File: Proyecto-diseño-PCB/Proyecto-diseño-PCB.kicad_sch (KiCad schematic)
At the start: 28 parts, among them J1 PROGRAMACIÓN/DEPURACIÓN, J2 USB_B_Micro, J3 Conn_01x13_Pin, J4 Conn_01x13_Pin, SW1 RESET, SW2 BOTON, SW3 BOTON, U1 PIC18LF45K50-I/P, U2 LP2950-3.3_TO92

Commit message: Correcciones
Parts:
- removed C7, C8: 1n, symbol Device:C
- added D4, D5: PESD3V3L4UG, Package_TO_SOT_SMD:SOT-353_SC-70-5, symbol Power_Protection:PESD3V3L4UG
- added FL1: BNX025, Filter:Filter_Murata_BNX025, symbol Filter:BNX025
- added R10, R11, R12, R13, R8, R9: 100, symbol Device:R_US
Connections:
- net BOTON1: now also D5.3 (K2), R8.2; no longer R6.1, SW2.1
- net BOTON2: now also D5.4 (K3), R9.2; no longer R7.1, SW3.1
- net GND: now also D4.2 (A), D5.2 (A), FL1.4 (CG); no longer J2.5 (GND)
- net MCLR: now also JP1.2 (B), R1.2, SW1.2, D5.1 (K1); no longer U1.1 (MCLR/VPP/RE3)
- net PGC: now also D4.4 (K3), R11.2; no longer J1.5 (Pin_5)
- net PGD: now also D4.5 (K4), R10.2; no longer J1.4 (Pin_4)
- net at J2.2 (D-): now also R12.2; no longer U1.23 (D-)
- net at J2.3 (D+): now also R13.2; no longer U1.24 (D+)
- net VIN: no longer names the net of C4.2, U2.3 (VI)
- net VIN: now also FL1.2 (CB); no longer J2.1 (VBUS), J3.14 (Pin_14)
- new net: R7.1, R9.1, SW3.1
- new net: R2.1, U1.1 (MCLR/VPP/RE3)
- new net: D4.3 (K2), R13.1, U1.24 (D+)
- new net: J1.4 (Pin_4), R10.1
- new net: J1.5 (Pin_5), R11.1
- new net: D4.1 (K1), R12.1, U1.23 (D-)
- new net: R6.1, R8.1, SW2.1
- new net 5V: FL1.1 (B), J2.1 (VBUS), J3.14 (Pin_14)
- new net MASA_SIN_FILTRAR: FL1.3 (PSG), J2.5 (GND)
- no-connect marks 1 -> 2
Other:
- note added: "Conectado a masa internamente"
- note added: "El PESD3V3L4UG es un integrado que cuenta con 4 TVS conectados a un anodo común. La conexión a masa solo está reperesntada en la unidad D#A."
- note removed: "Constante de tiempo DEBOUNCE = 100us"
- moved on the sheet: C4, C5, J2, R6, R7, SW2, SW3, U2

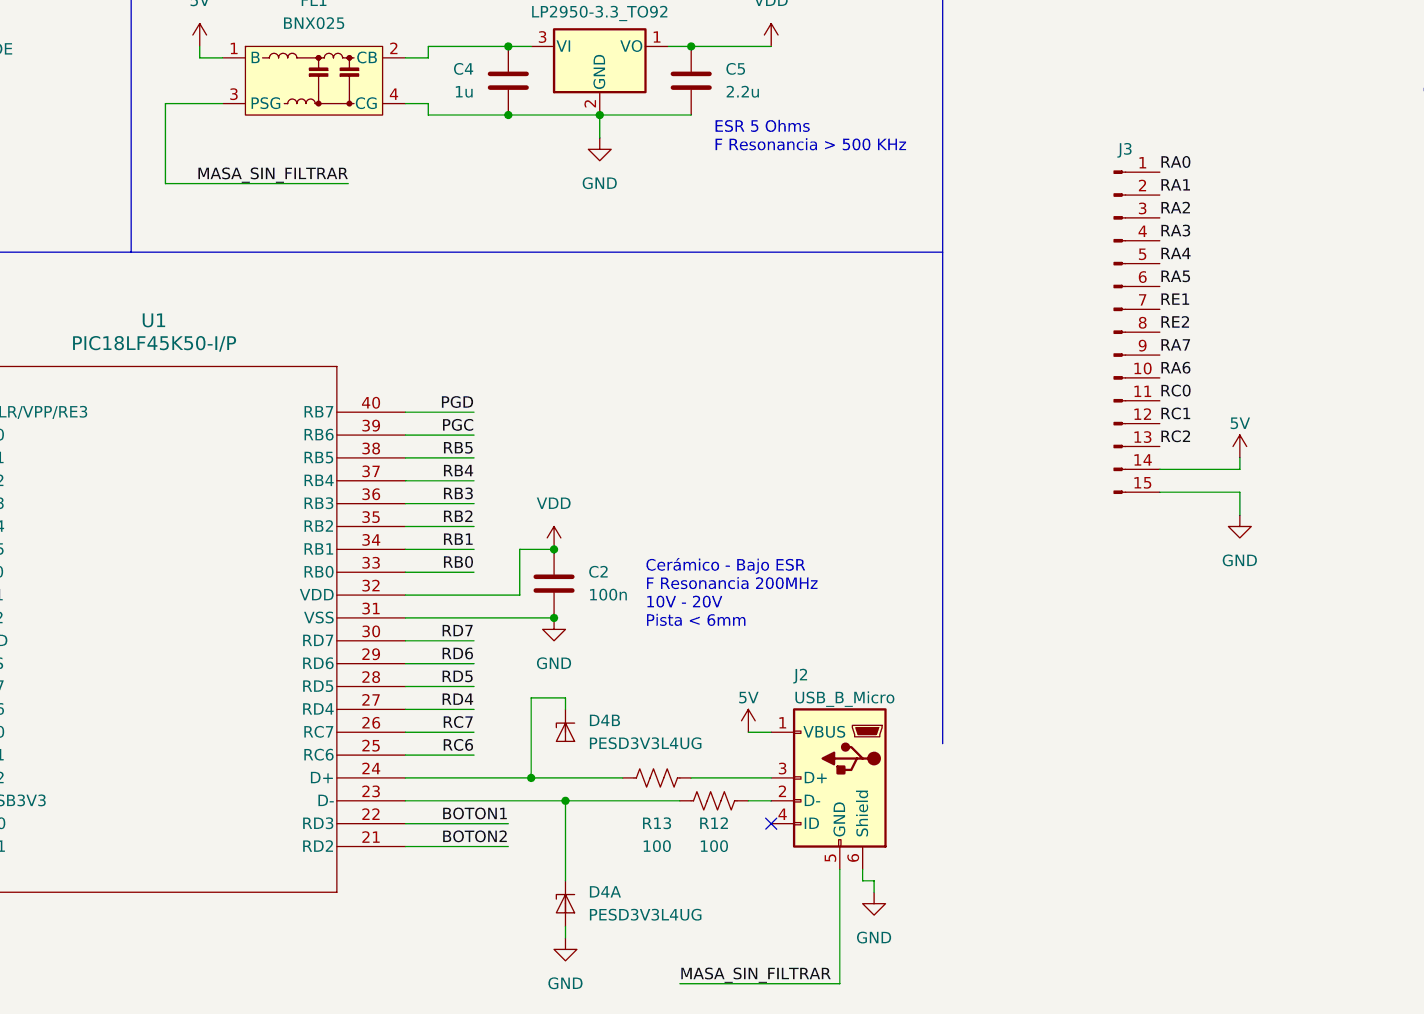
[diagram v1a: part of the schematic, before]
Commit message: fix: Cambio de nombre de net label
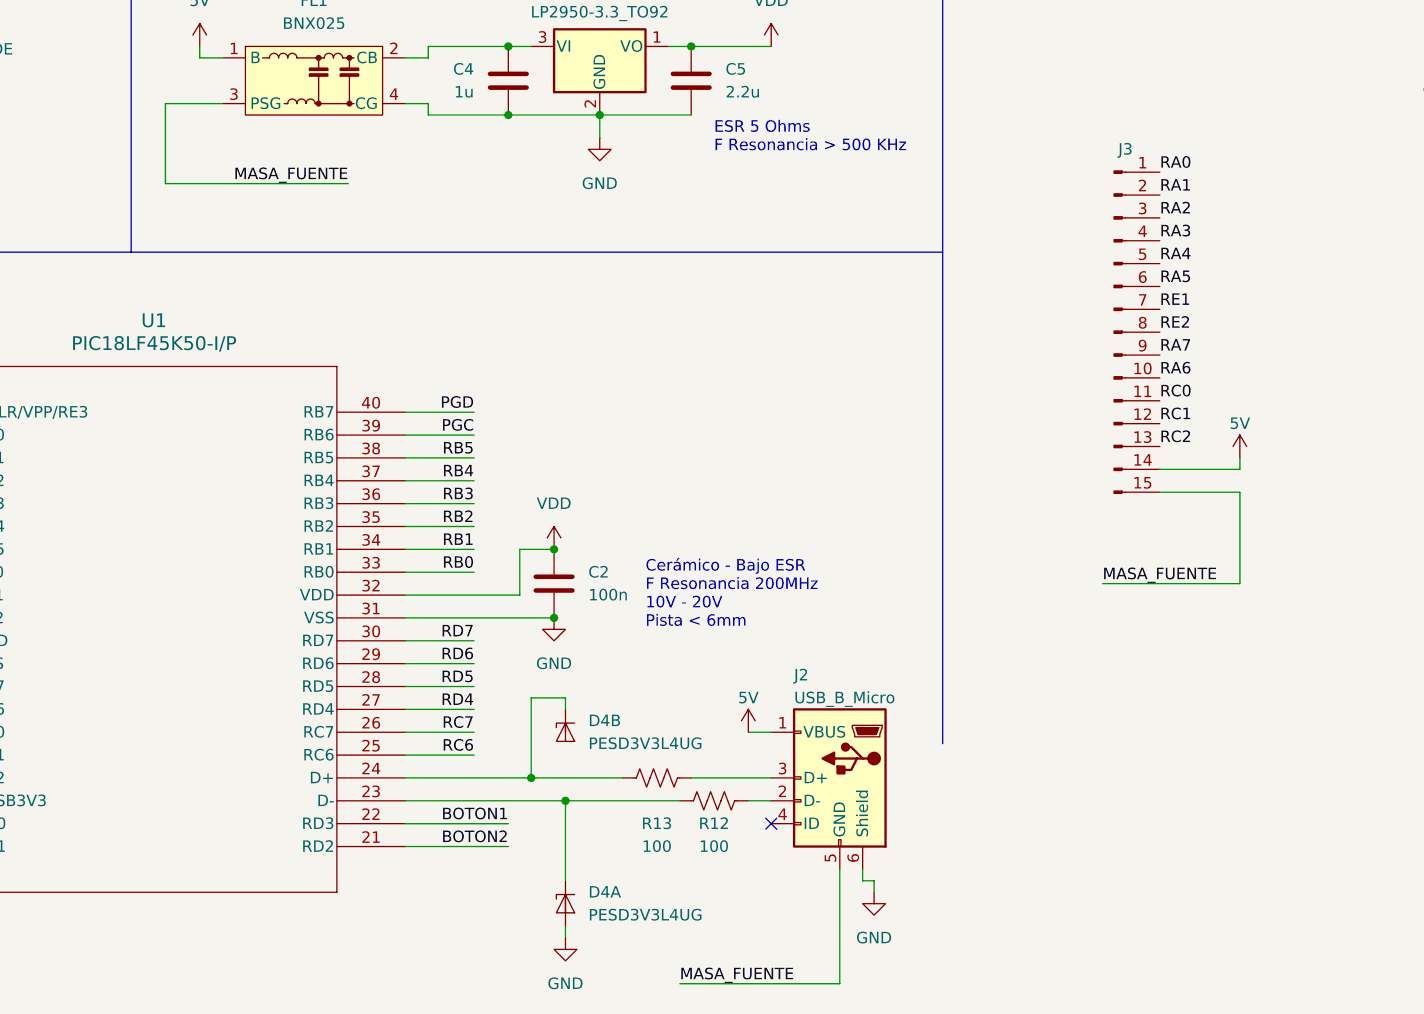
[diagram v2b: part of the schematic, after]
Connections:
- net GND: no longer J3.15 (Pin_15)
- net MASA_SIN_FILTRAR renamed MASA_FUENTE
- net MASA_FUENTE: now also J3.15 (Pin_15)
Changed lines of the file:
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@@
 	(wire
 		(pts
+			(xy 195.58 147.32) (xy 210.82 147.32)
+		)
+		(stroke
+			(width 0)
+			(type default)
+		)
+	)
+	(wire
+		(pts
 			(xy 53.34 173.99) (xy 62.23 173.99)
 		)
@@
 	(wire
 		(pts
-			(xy 210.82 137.16) (xy 210.82 139.7)
+			(xy 210.82 137.16) (xy 210.82 147.32)
 		)
 		(stroke
@@
 		)
 	)
-	(label "MASA_SIN_FILTRAR"
+	(label "MASA_FUENTE"
 		(at 148.59 191.77 0)
 		(effects
@@
 		)
 	)
-	(label "MASA_SIN_FILTRAR"
+	(label "MASA_FUENTE"
 		(at 111.76 102.87 180)
 		(effects
@@
 		)
 	)
+	(label "MASA_FUENTE"
+		(at 195.58 147.32 0)
+		(fields_autoplaced yes)
+		(effects
+			(font
+				(size 1.27 1.27)
+			)
+			(justify left bottom)
+		)
+		(property "Netclass" "ALIMENTACION"
+			(at 195.58 148.59 0)
+			(effects
+				(font
+					(size 1.27 1.27)
+					(italic yes)
+				)
+				(justify left)
+				(hide yes)
+			)
+		)
+	)
 	(label "RC2"
 		(at 54.61 168.91 0)
@@
 					(unit 1)
 				)
-			)
-		)
-	)
-	(symbol
-		(lib_id "power:GND")
-		(at 210.82 139.7 0)
-		(unit 1)
-		(exclude_from_sim no)
-		(in_bom yes)
-		(on_board yes)
-		(dnp no)
-		(fields_autoplaced yes)
-		(property "Reference" "#PWR025"
-			(at 210.82 146.05 0)
-			(effects
-				(font
-					(size 1.27 1.27)
-				)
-				(hide yes)
-			)
-		)
-		(property "Value" "GND"
-			(at 210.82 144.78 0)
-			(effects
-				(font
-					(size 1.27 1.27)
-				)
-			)
-		)
-		(property "Footprint" ""
-			(at 210.82 139.7 0)
-			(effects
-				(font
-					(size 1.27 1.27)
-				)
-				(hide yes)
-			)
-		)
-		(property "Datasheet" ""
-			(at 210.82 139.7 0)
-			(effects
-				(font
-					(size 1.27 1.27)
-				)
-				(hide yes)
-			)
-		)
-		(property "Description" "Power symbol creates a global label with name \"GND\" , ground"
-			(at 210.82 139.7 0)
-			(effects
-				(font
-					(size 1.27 1.27)
-				)
-				(hide yes)
-			)
-		)
-		(pin "1"
-		)
-		(instances
-			(project "Proyecto-diseño-PCB"
-				(path "/07fbb56e-f9f5-495b-a4b8-be8a0cd3547b"
-					(reference "#PWR025")
-					(unit 1)
-				)

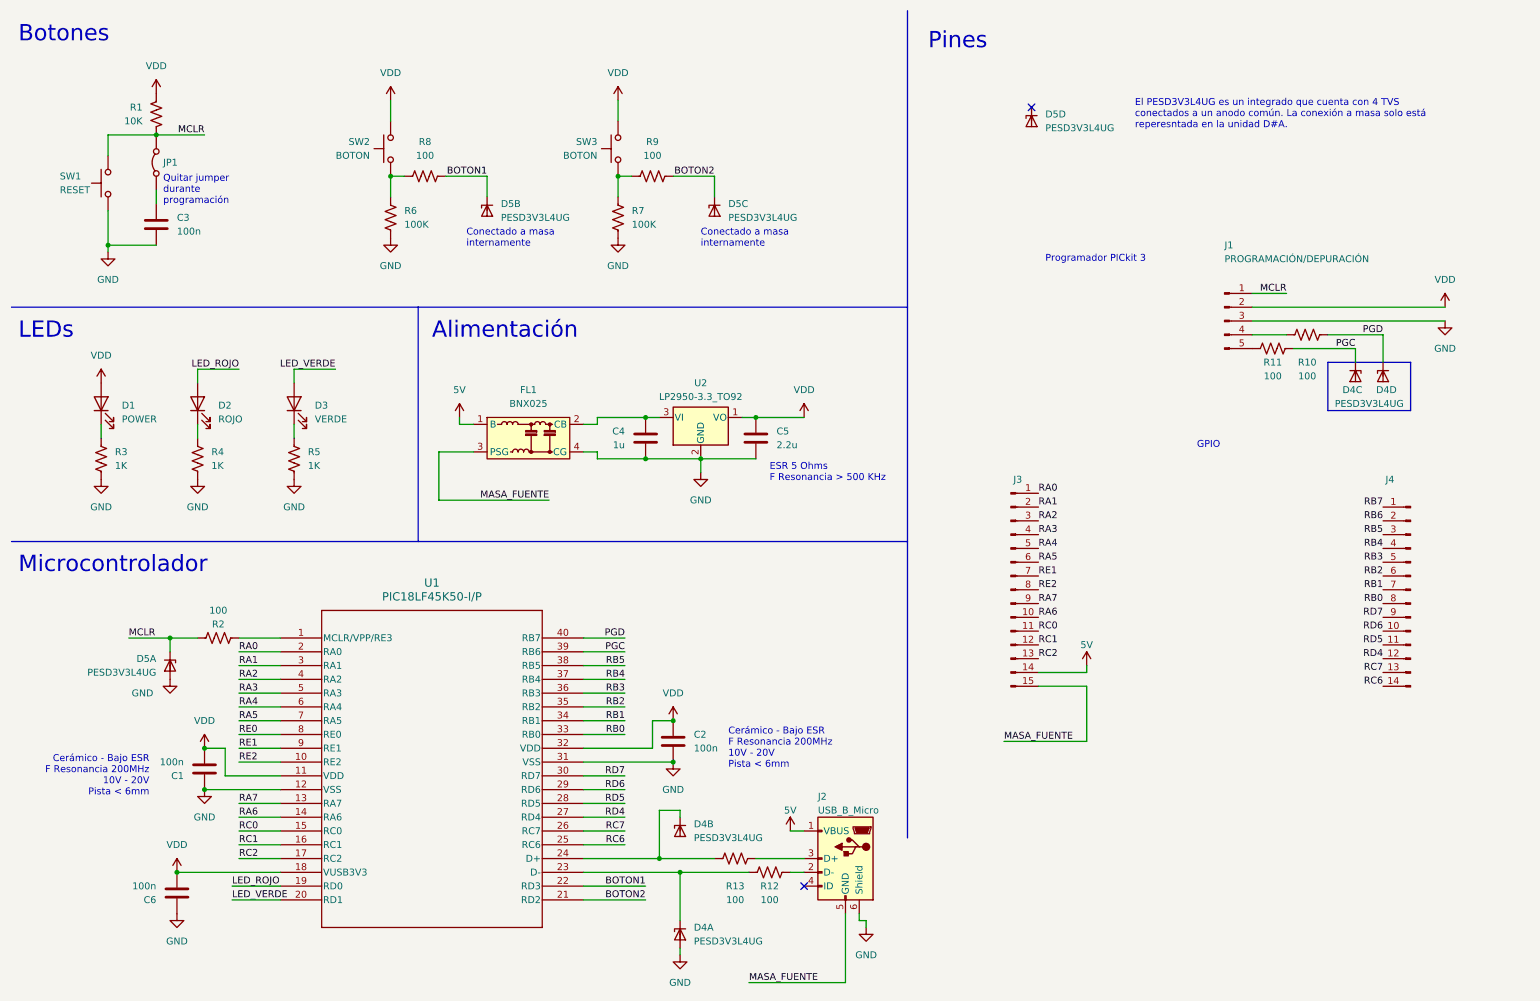
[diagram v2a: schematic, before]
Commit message: fix: protección ESD
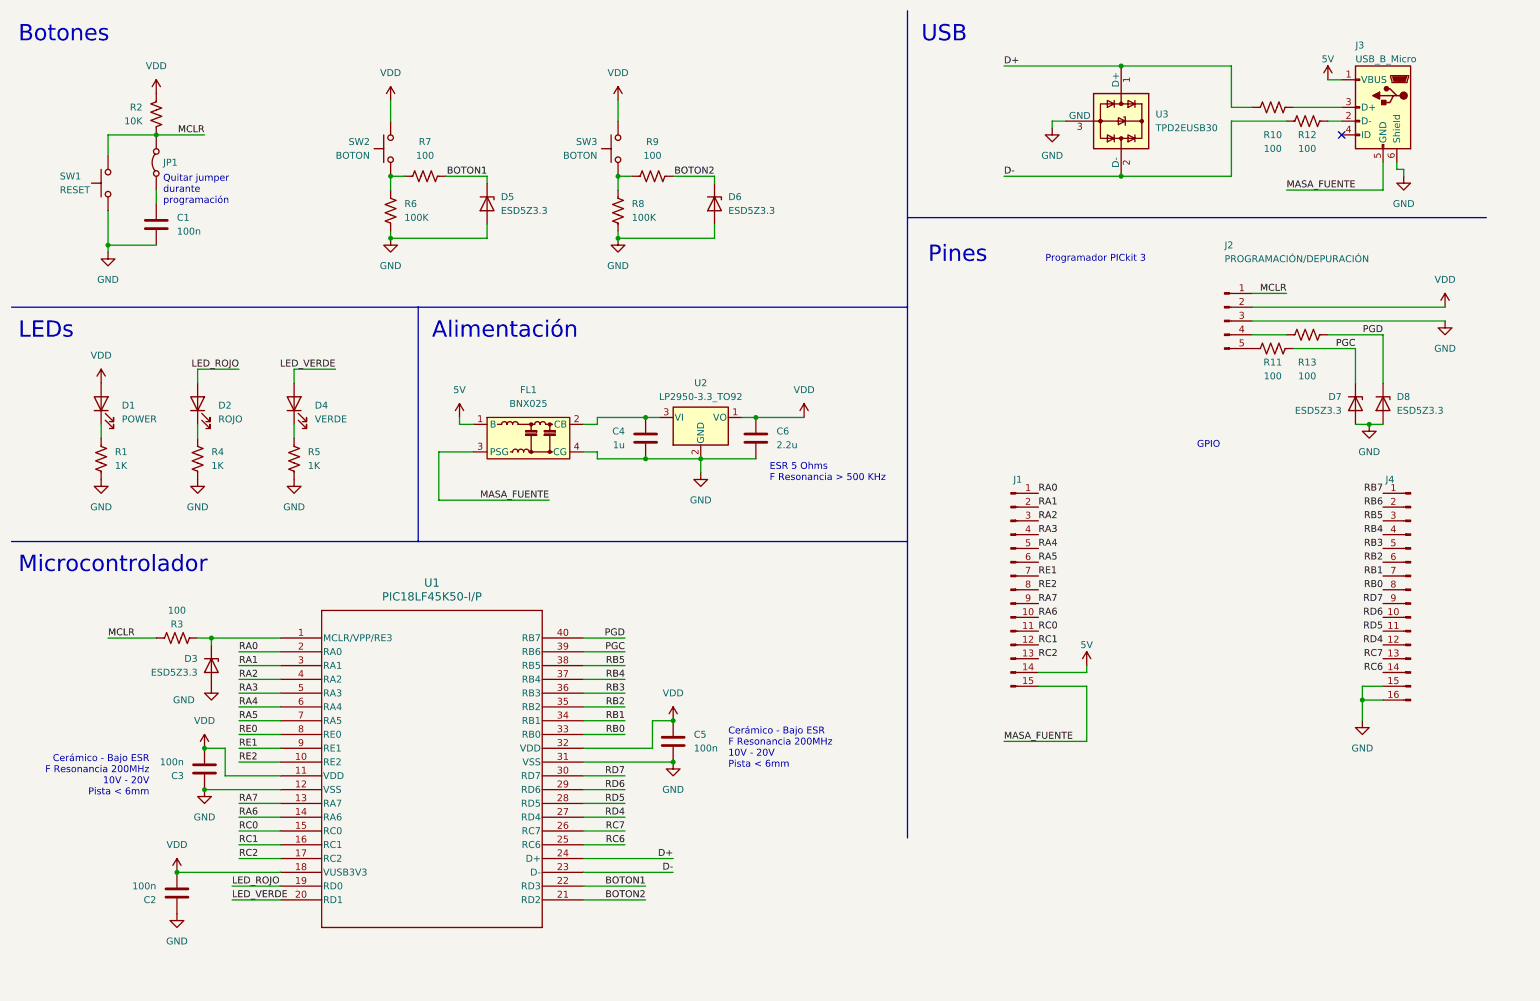
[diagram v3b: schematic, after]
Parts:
- removed D4, D5: PESD3V3L4UG, Package_TO_SOT_SMD:SOT-353_SC-70-5, symbol Power_Protection:PESD3V3L4UG
- added D3, D5, D6, D7, D8: ESD5Z3.3, Diode_SMD:D_SOD-523, symbol Diode:ESD5Zxx
- added U3: TPD2EUSB30, Package_TO_SOT_SMD:Texas_DRT-3, symbol Power_Protection:TPD2EUSB30
- J4: symbol Connector:Conn_01x14_Pin -> Connector:Conn_01x16_Pin
- renumbered C3 to C1, C6 to C2, C1 to C3, C2 to C5, C5 to C6, D3 to D4, J3 to J1, J1 to J2, J2 to J3, R3 to R1, R13 to R10, R10 to R13, R1 to R2, R2 to R3, R8 to R7, R7 to R8
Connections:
- net BOTON1: now also D5.1 (K)
- net BOTON2: now also D6.1 (K)
- net GND: now also J4.15 (Pin_15), J4.16 (Pin_16), D3.2 (A), D5.2 (A), D6.2 (A), D7.2 (A), D8.2 (A), U3.3 (GND)
- net PGC: now also D7.1 (K)
- net PGD: now also D8.1 (K)
- net at R3.1, U1.1 (MCLR/VPP/RE3): now also D3.1 (K)
- net D+: now reaches R10.1, U1.24 (D+)
- net D+: now also U3.1 (D+)
- net D-: now reaches R12.1, U1.23 (D-)
- net D-: now also U3.2 (D-)
- no-connect marks 2 -> 1
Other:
- note added: "USB"
- note removed: "Conectado a masa internamente"
- note removed: "El PESD3V3L4UG es un integrado que cuenta con 4 TVS conectados a un anodo común. La conexión a masa solo está reperesntada en la unidad D#A."
- moved on the sheet: J3, R10, R12, R3, R6, R8

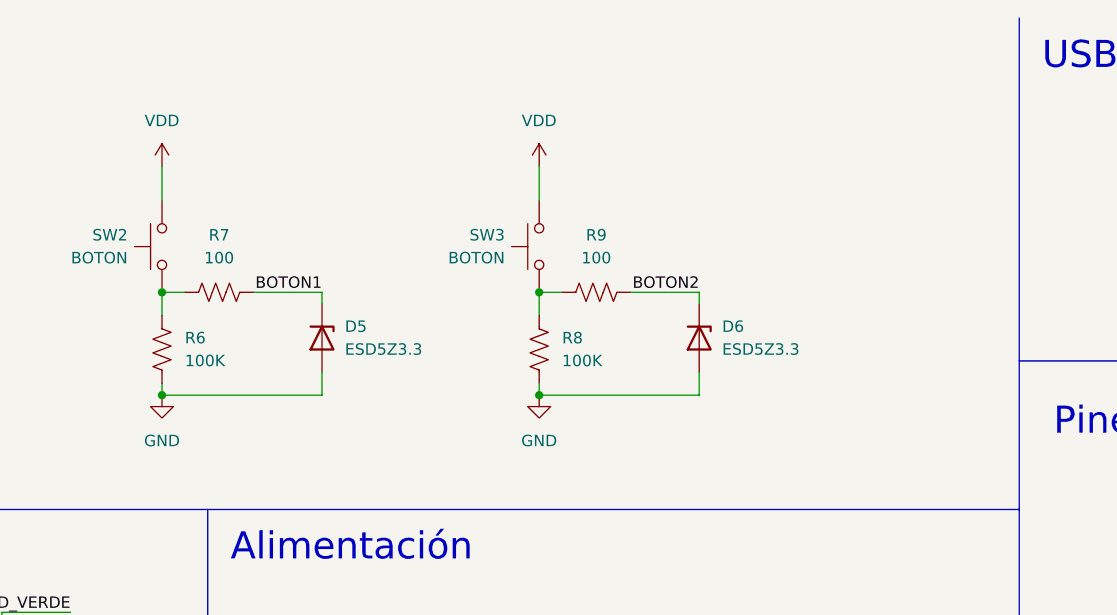
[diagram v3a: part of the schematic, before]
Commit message: capacitores de filtro en pines de botones de entrada
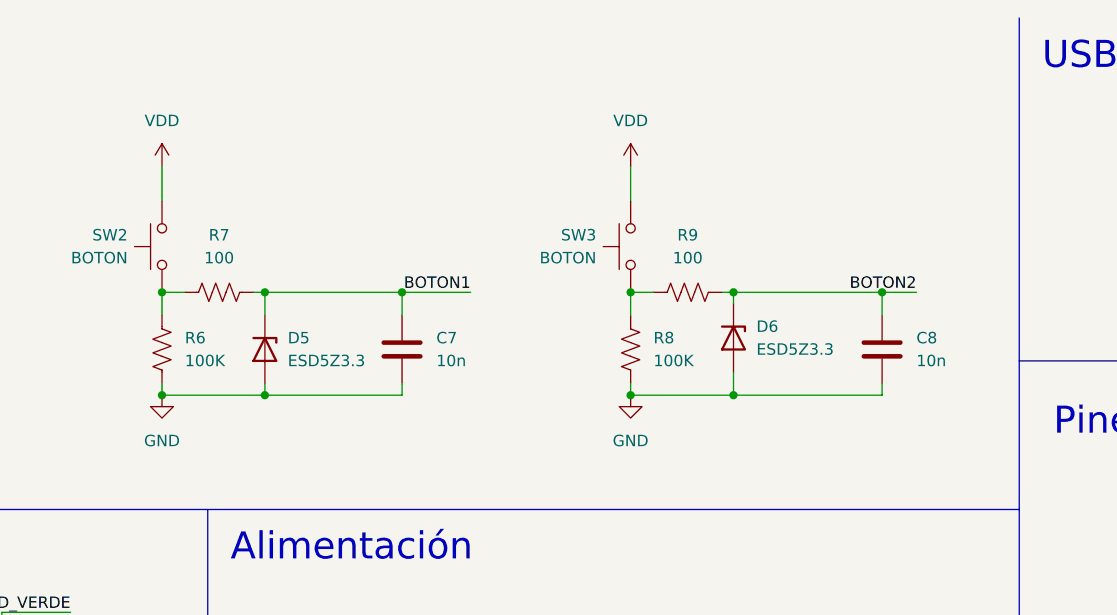
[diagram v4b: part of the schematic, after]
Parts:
- added C7, C8: 10n, symbol Device:C
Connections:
- net BOTON1: now also C7.1
- net BOTON2: now also C8.1
- net GND: now also C7.2, C8.2
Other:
- moved on the sheet: D5, D6, R8, R9, SW3
